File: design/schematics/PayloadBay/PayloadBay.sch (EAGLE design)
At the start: 25 parts, among them IC1 MC33269ST-5.0T3, IC2 MC33269D-5.0, IC3 ATMEGA2560-16AU, Q2 16MHz, X1 DC21MMX, Y1 16MHz

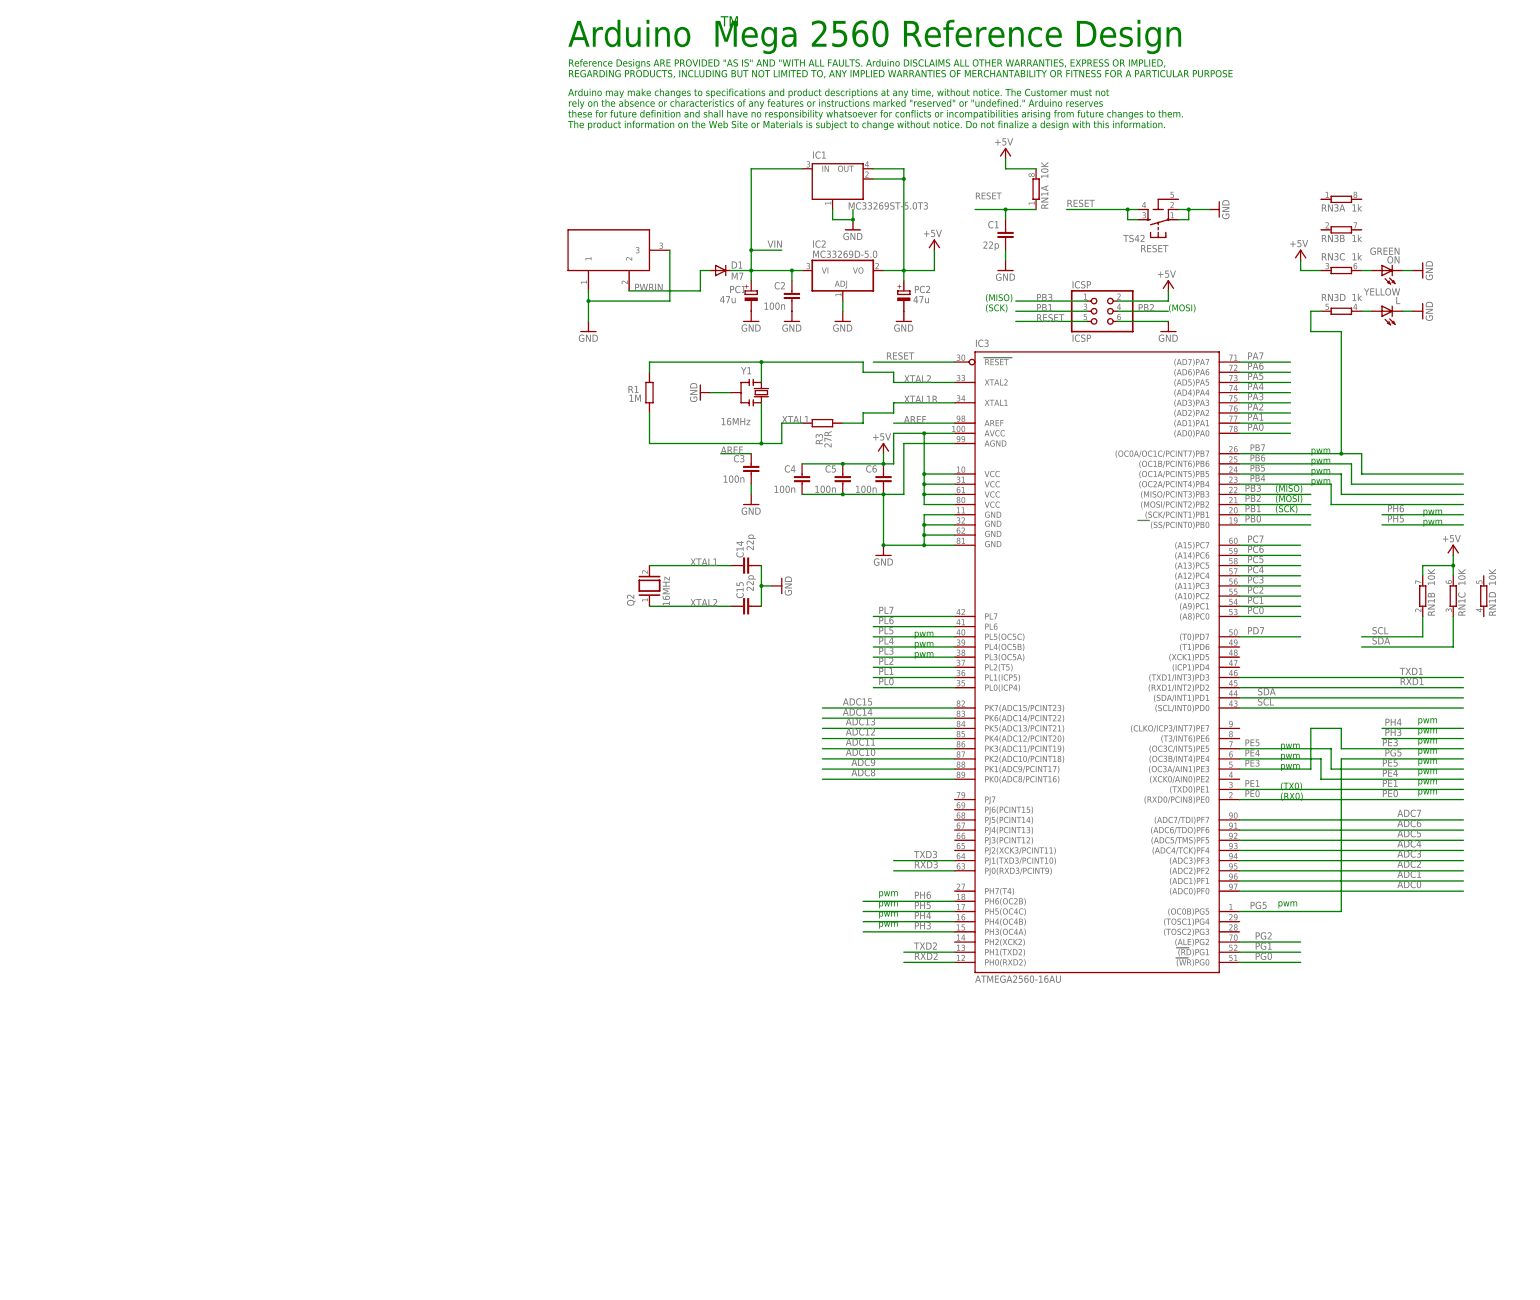
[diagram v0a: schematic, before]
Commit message: updated schematic
added subfolders and eagle project files
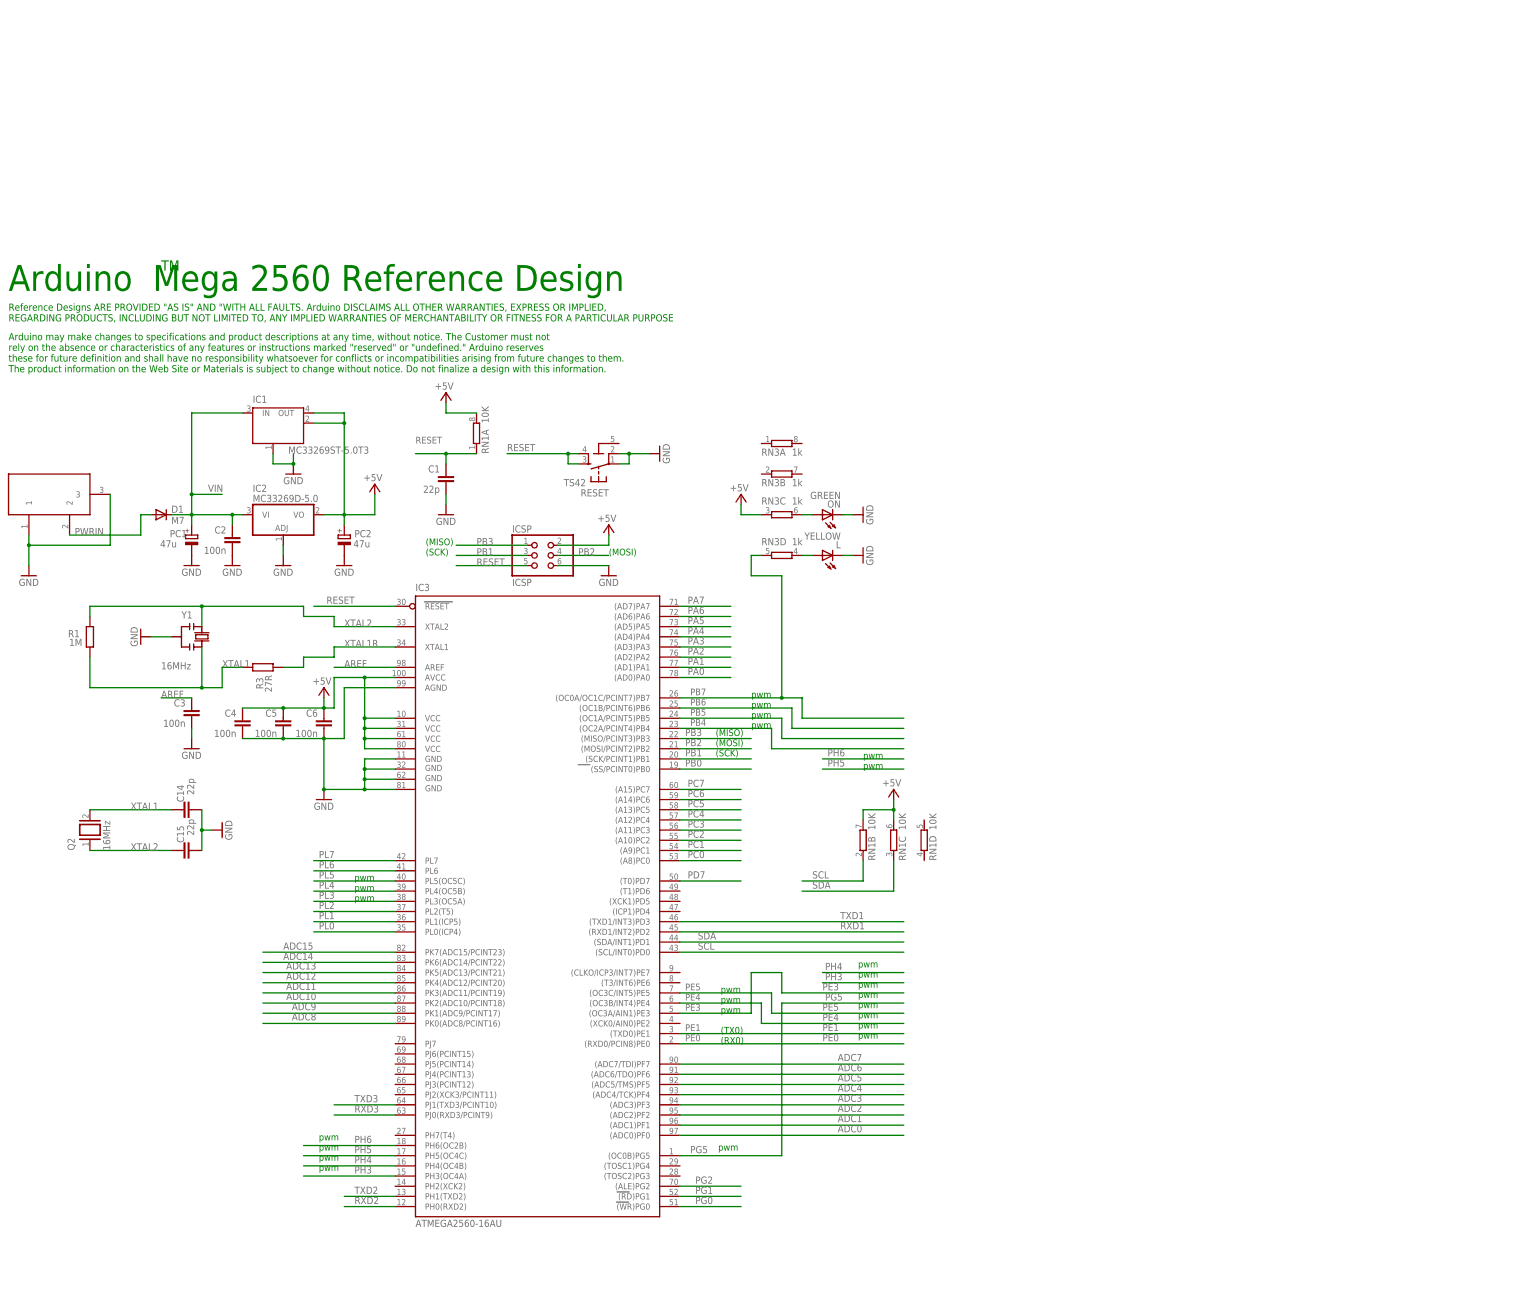
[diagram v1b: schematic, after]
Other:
- moved on the sheet: C1, C14, C15, C2, C3, C4, C5, C6, D1, IC1, IC2, IC3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

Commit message: Updated payload bay schematic
* added text, reed switch, limit switches, mosfet, and motor
* added png version of schematic
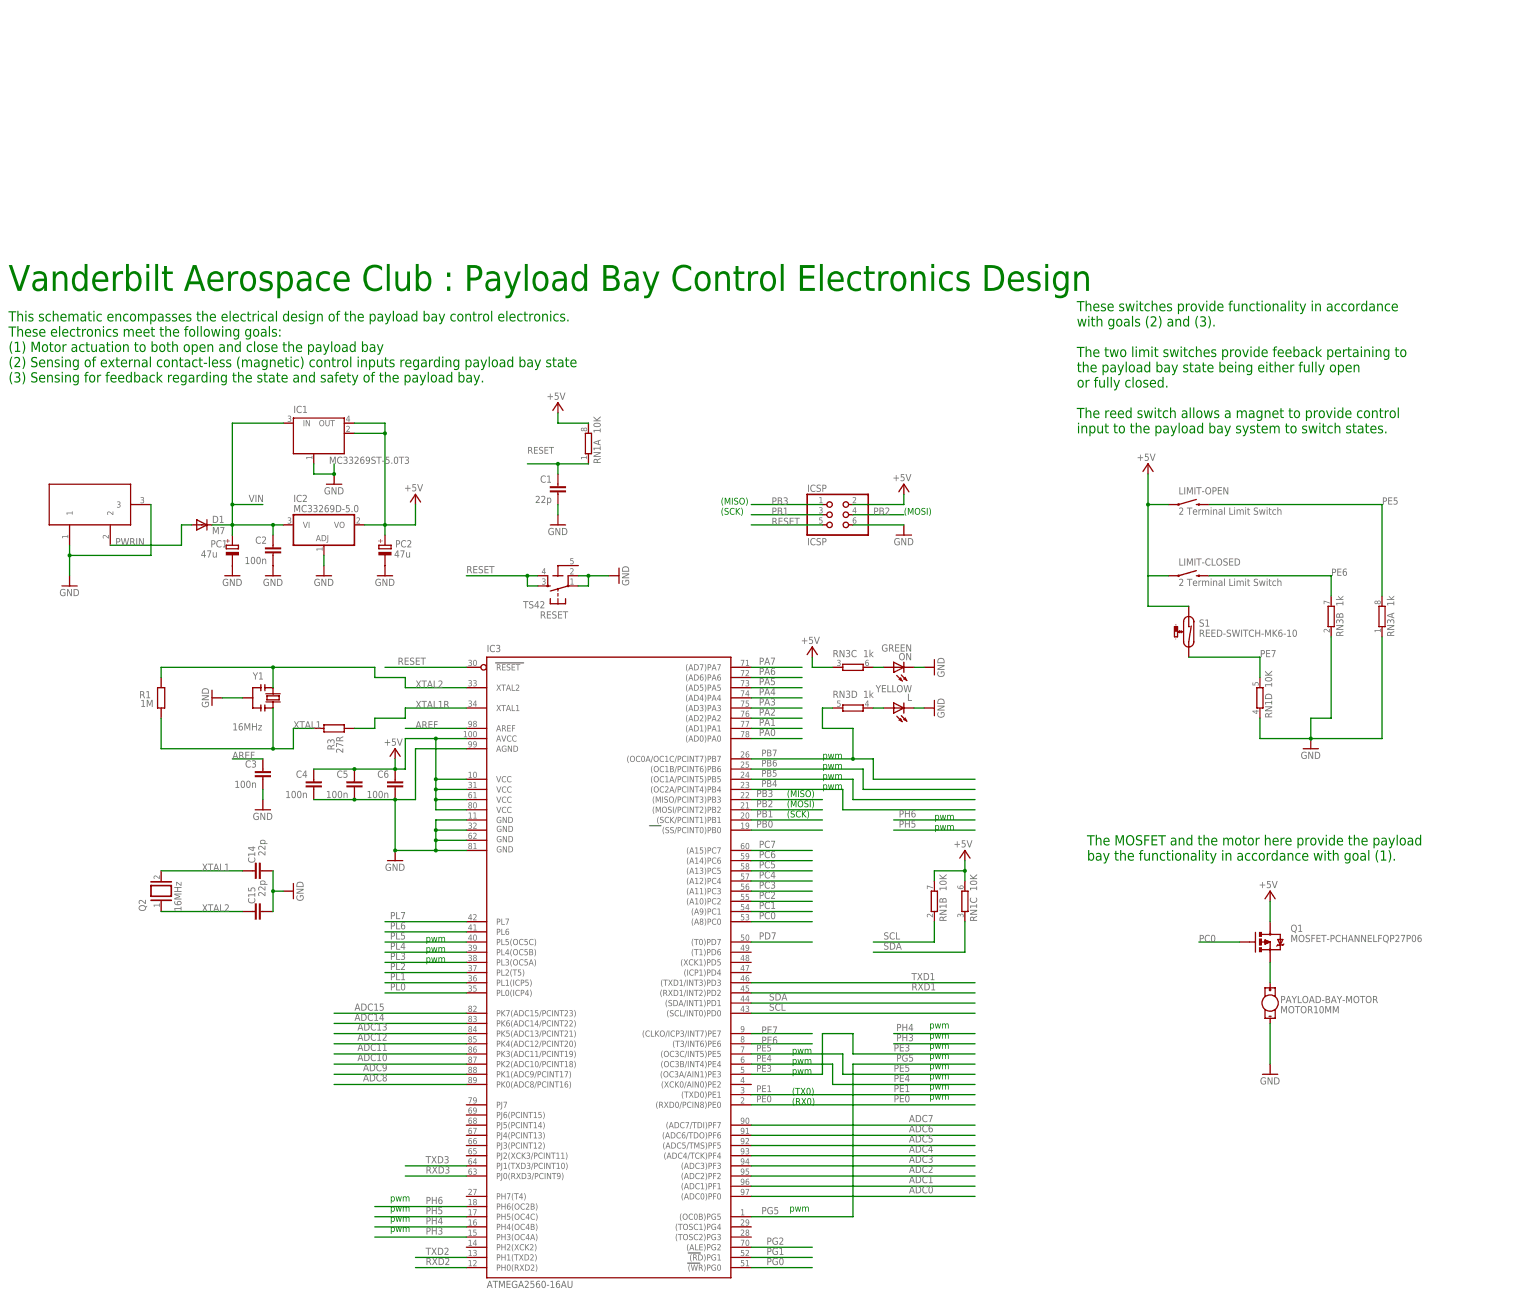
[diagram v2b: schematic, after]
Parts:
- added LIMIT-CLOSED, LIMIT-OPEN: 2 Terminal Limit Switch, SparkFun-Electromechanical:SWITCH-MOMENTARY-212MM
- added PAYLOAD-BAY-MOTOR: MOTOR10MM, SparkFun-Electromechanical:MOTOR10MM
- added Q1: MOSFET-PCHANNELFQP27P06, SparkFun-DiscreteSemi:MOSFET-PCHANNELFQP27P06
- added S1: REED-SWITCH-MK6-10, switch-reed:REED-SWITCH-MK6-10
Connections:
- new net N$1: PAYLOAD-BAY-MOTOR.+, Q1.S
- new net PE6: IC3.(T3/INT6)PE6, LIMIT-CLOSED.2, RN3B.2
- new net PE7: IC3.(CLKO/ICP3/INT7)PE7, RN1D.2, S1.2
- net +5V: now also LIMIT-CLOSED.1, LIMIT-OPEN.1, Q1.D, S1.1
- net GND: now also PAYLOAD-BAY-MOTOR.-, RN1D.1, RN3A.1, RN3B.1
- net PC0: now also Q1.G
- net PE5: now also LIMIT-OPEN.2, RN3A.2
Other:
- note added: "The MOSFET and the motor here provide the payload bay the functionality in accordance with goal (1)."
- note added: "These switches provide functionality in accordance with goals (2) and (3). The two limit switches provide feeback pertaining to the payload bay state being either fully open or fully closed. The reed switch allows a magnet to provide control input to the payload bay system to switch states."
- note added: "This schematic encompasses the electrical design of the payload bay control electronics. These electronics meet the following goals: (1) Motor actuation to both open and close the payload bay (2) Sensing of external contact-less (magnetic) control inputs regarding payload bay state (3) Sensing for feedback regarding the state and safety of the payload bay."
- note added: "Vanderbilt Aerospace Club : Payload Bay Control Electronics Design"
- note removed: "Arduino Mega 2560 Reference Design"
- note removed: "Arduino may make changes to specifications and product descriptions at any time, without notice. The Customer must not rely on the absence or characteristics of any features or instructions marked "reserved" or "undefined." Arduino reserves these for future definition and shall have no responsibility whatsoever for conflicts or incompatibilities arising from future changes to them. The product in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"
- note removed: "Reference Designs ARE PROVIDED "AS IS" AND "WITH ALL FAULTS. Arduino DISCLAIMS ALL OTHER WARRANTIES, EXPRESS OR IMPLIED, REGARDING PRODUCTS, INCLUDING BUT NOT LIMITED TO, ANY IMPLIED WARRANTIES OF MERCHANTABILITY OR FITNESS FOR A PARTICULAR PURPOSE"
- note removed: "TM"
- moved on the sheet: C1, C14, C15, C2, C3, C4, C5, C6, D1, IC1, IC2, IC3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
